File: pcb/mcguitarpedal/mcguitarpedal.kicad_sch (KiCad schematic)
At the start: 52 parts, among them J1 IN, J10 ENCODER2, J11 ENCODER3, J2 PREAMP_HEADERS, J3 BTN_MTX, J4 OUT, J5 EXP, J6 ILI9488 Module, J7 PWR_IN, J8 POT_HP_VOLUME_10k, J9 ENCODER1, SW1 SW_BYPASS, SW5 SW_TUNER, SW6 SW_PRESET, U1 Teensy4.0_AudioShield_REVD, U2 Teensy4.1, U4 74HC148, U5 74HC4094, U6 STPDWN-3P-5V, U7 STDN-3A24-ADJ

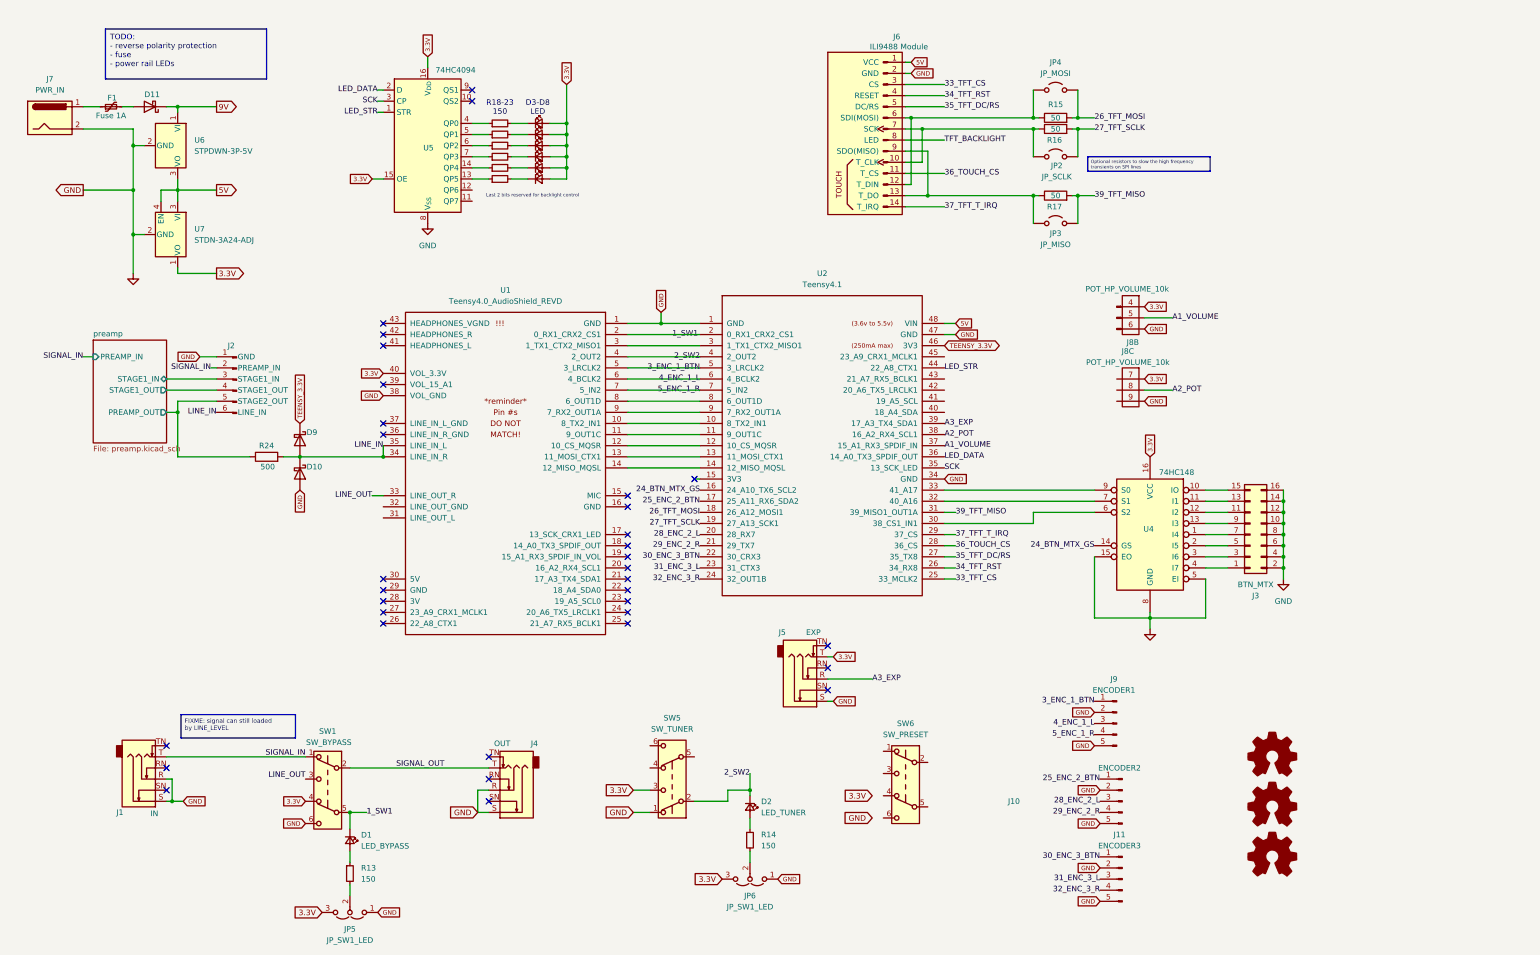
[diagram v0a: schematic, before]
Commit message: HCT595, audio shield sockets
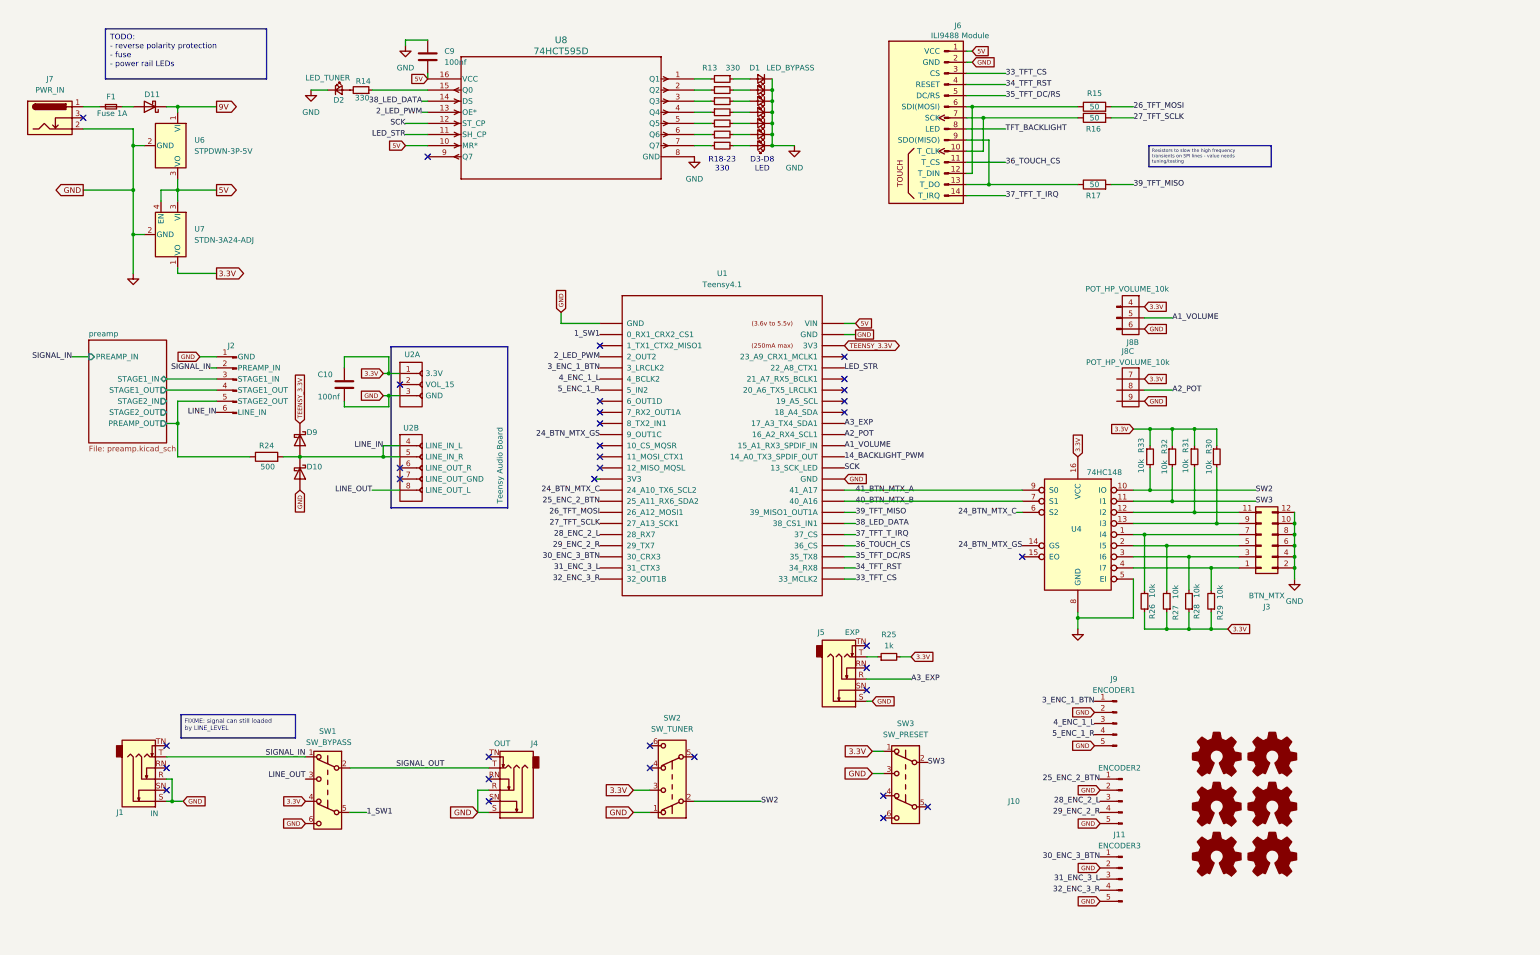
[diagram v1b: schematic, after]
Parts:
- removed D3: LED, LED_THT:LED_D3.0mm, symbol Device:LED_Small
- removed JP2: JP_SCLK, Connector_PinHeader_2.54mm:PinHeader_1x02_P2.54mm_Vertical, symbol Jumper:Jumper_2_Open
- removed JP3: JP_MISO, Connector_PinHeader_2.54mm:PinHeader_1x02_P2.54mm_Vertical, symbol Jumper:Jumper_2_Open
- removed JP4: JP_MOSI, Connector_PinHeader_2.54mm:PinHeader_1x02_P2.54mm_Vertical, symbol Jumper:Jumper_2_Open
- removed JP5, JP6: JP_SW1_LED, Connector_PinHeader_2.54mm:PinHeader_1x03_P2.54mm_Vertical, symbol Jumper:Jumper_3_Open
- removed U1: Teensy4.0_AudioShield_REVD, teensy_audio_shield:4.0audioshield_reference, symbol Audio board:Teensy4.0_AudioShield_REVD
- removed U5: 74HC4094, TI_FOOTPRINTS:N16, symbol 4xxx:HEF4094B
- added C10, C9: 100nf, Capacitor_THT:C_Rect_L7.2mm_W2.5mm_P5.00mm_FKS2_FKP2_MKS2_MKP2, symbol Device:C
- added D6: LED, mcguitarpedal:LED_D3.0mm, symbol Device:LED_Small
- added ENC1, ENC2, ENC3: Logo_Open_Hardware_Small, mcguitarpedal:Floating Encoder, symbol Graphic:Logo_Open_Hardware_Small
- added R25: 1k, Resistor_THT:R_Axial_DIN0207_L6.3mm_D2.5mm_P7.62mm_Horizontal, symbol Device:R_Small
- added R26, R27, R28, R29, R30, R31, R32, R33: 10k, Resistor_SMD:R_1206_3216Metric_Pad1.30x1.75mm_HandSolder, symbol Device:R_Small
- added U2: Teensy Audio Board, mcguitarpedal:4.0audioshield, symbol mcguitarpedal:Teensy_Audio_Board_Secondary_Sockets
- added U8: 74HCT595D, TI_FOOTPRINTS:SOT109-1_NEX, symbol 74HCT595:74HCT595D
- D3: renamed from D6; footprint LED_THT:LED_D3.0mm -> mcguitarpedal:LED_D3.0mm
- D4: renamed from D5; footprint LED_THT:LED_D3.0mm -> mcguitarpedal:LED_D3.0mm
- D5: renamed from D4; footprint LED_THT:LED_D3.0mm -> mcguitarpedal:LED_D3.0mm
- D7, D8: footprint LED_THT:LED_D3.0mm -> mcguitarpedal:LED_D3.0mm
- F1: footprint (none) -> Fuse:Fuse_Littelfuse_395Series; symbol Device:Polyfuse_Small -> Device:Fuse_Small
- J3: footprint Connector_PinHeader_2.54mm:PinHeader_2x08_P2.54mm_Vertical -> Connector_PinHeader_2.54mm:PinHeader_2x06_P2.54mm_Vertical; symbol Connector_Generic:Conn_02x08_Odd_Even -> Connector_Generic:Conn_02x06_Odd_Even
- J7: symbol Connector:Barrel_Jack -> Connector:Barrel_Jack_Switch
- R13, R14, R22, R23: value 150 -> 330
- R18: renamed from R21; value 150 -> 330
- R19: renamed from R20; value 150 -> 330
- R20: renamed from R19; value 150 -> 330
- R21: renamed from R18; value 150 -> 330
- renumbered SW5 to SW2, SW6 to SW3, U2 to U1
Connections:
- net 1_SW1: no longer D1.1 (K)
- net 24_BTN_MTX_GS: now also U1.11 (9_OUT1C); no longer U1.16 (24_A10_TX6_SCL2)
- net 3.3V: now also SW3.1 (A), C10.1, R25.2, R26.1, R27.1, R28.1, R29.1, R30.1, R31.1, R32.1, R33.1, U2.1 (3.3V); no longer D3.2 (A), D4.2 (A), D5.2 (A), D7.2 (A), D8.2 (A), J5.T
- net 5V: now also C9.2, U8.10 (MR*), U8.16 (VCC)
- net GND: now also D1.1 (K), D2.1 (K), D3.1 (K), D4.1 (K), D5.1 (K), D7.1 (K), D8.1 (K), SW3.3 (C), C10.2, C9.1, D6.1 (K), U2.3 (GND), U8.8 (GND); no longer J3.14 (Pin_14), J3.16 (Pin_16), U4.15 (EO)
- net LED_STR: now also U8.11 (SH_CP)
- net LINE_IN: now also U2.4 (LINE_IN_L), U2.5 (LINE_IN_R)
- net LINE_OUT: now also U2.8 (LINE_OUT_L)
- net SCK: now also U8.12 (ST_CP)
- net at D2.2 (A): now also R14.2; no longer R14.1
- net at R18.1: now also U8.7 (Q7)
- net at R18.2: now also D3.2 (A); no longer D3.1 (K)
- net at R22.1: now also U8.3 (Q3)
- net at R22.2: now also D7.2 (A); no longer D7.1 (K)
- net at R20.1: now also U8.5 (Q5)
- net at R20.2: now also D5.2 (A); no longer D5.1 (K)
- net SW3: now reaches SW3.2 (B)
- net SW3: now also U4.11 (I1), R32.2
- net at R13.2: now also U8.1 (Q1)
- net at R23.1: now also U8.2 (Q2)
- net at R23.2: now also D8.2 (A); no longer D8.1 (K)
- net 24_BTN_MTX_C: now reaches U4.6 (S2)
- net 24_BTN_MTX_C: now also U1.16 (24_A10_TX6_SCL2); no longer U1.30 (38_CS1_IN1)
- net 40_BTN_MTX_B: now reaches U1.32 (40_A16), U4.7 (S1)
- net 41_BTN_MTX_A: now reaches U1.33 (41_A17), U4.9 (S0)
- net at R21.1: now also U8.4 (Q4)
- net at R19.1: now also U8.6 (Q6)
- net at R19.2: now also D4.2 (A); no longer D4.1 (K)
- net at J3.7 (Pin_7), U4.1 (I4): now also R26.2
- net SW2: now reaches U4.10 (IO)
- net SW2: now also SW2.2 (B), R33.2; no longer J3.15 (Pin_15)
- net at J3.11 (Pin_11), U4.12 (I2): now also R31.2
- net at J3.9 (Pin_9), U4.13 (I3): now also R30.2
- net at J3.5 (Pin_5), U4.2 (I5): now also R27.2
- net at J3.3 (Pin_3), U4.3 (I6): now also R28.2
- net at J3.1 (Pin_1), U4.4 (I7): now also R29.2
- net at R21.2: now also D6.2 (A)
- removed net 2_SW2: D2.1 (K), SW2.2 (B), U1.4 (2_OUT2)
- net LED_DATA renamed 14_BACKLIGHT_PWM
- new net: R14.1, U8.15 (Q0)
- new net: J5.T, R25.1
- new net 2_LED_PWM: U1.4 (2_OUT2), U8.13 (OE*)
- new net 38_LED_DATA: U1.30 (38_CS1_IN1), U8.14 (DS)
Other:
- sheet preamp ports: added STAGE2_IN, STAGE2_OUT; removed none
- note added: "R18-23 330"
- note removed: "R18-23 150"
- moved on the sheet: D1, D2, J5, J6, R13, R14, R15, R16, R17, U4

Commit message: Miniaturization
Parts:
- added Q1: 2N7002K, Package_TO_SOT_SMD:SOT-23, symbol Transistor_FET:2N7002K
- added R36, R37, R38: 100, Resistor_THT:R_Axial_DIN0207_L6.3mm_D2.5mm_P7.62mm_Horizontal, symbol Device:R_Small
- added SW5, SW6: SW_PWR, Connector_PinHeader_2.54mm:PinHeader_1x02_P2.54mm_Vertical, symbol Switch:SW_SPST
- U6: footprint Package_TO_SOT_THT:TO-220-3_Vertical -> Package_TO_SOT_THT:TO-220-3_Horizontal_TabDown
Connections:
- net 14_BACKLIGHT_PWM: now also R37.1
- net 5V: now also SW6.2 (B)
- net GND: now also Q1.2 (S)
- net TFT_BACKLIGHT: now also R38.2
- net at F1.1: now also SW5.2 (B); no longer J7.1
- new net: R38.1, SW6.1 (A)
- new net: Q1.1 (G), R37.2
- new net: Q1.3 (D), R36.1
- new net: J7.1, SW5.1 (A)
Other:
- moved on the sheet: D11, D2, F1, J7, R14, U6, U7

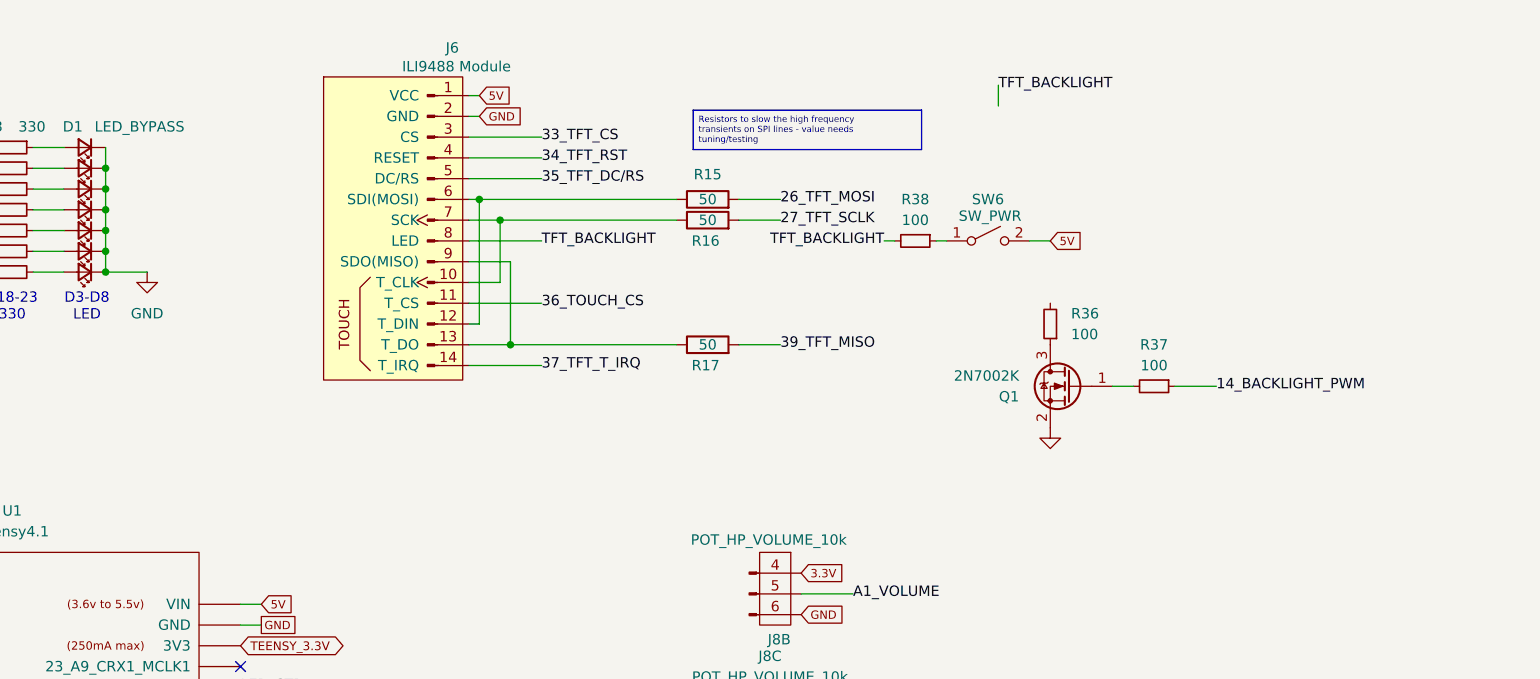
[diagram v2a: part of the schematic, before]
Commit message: Display backlight control schematic
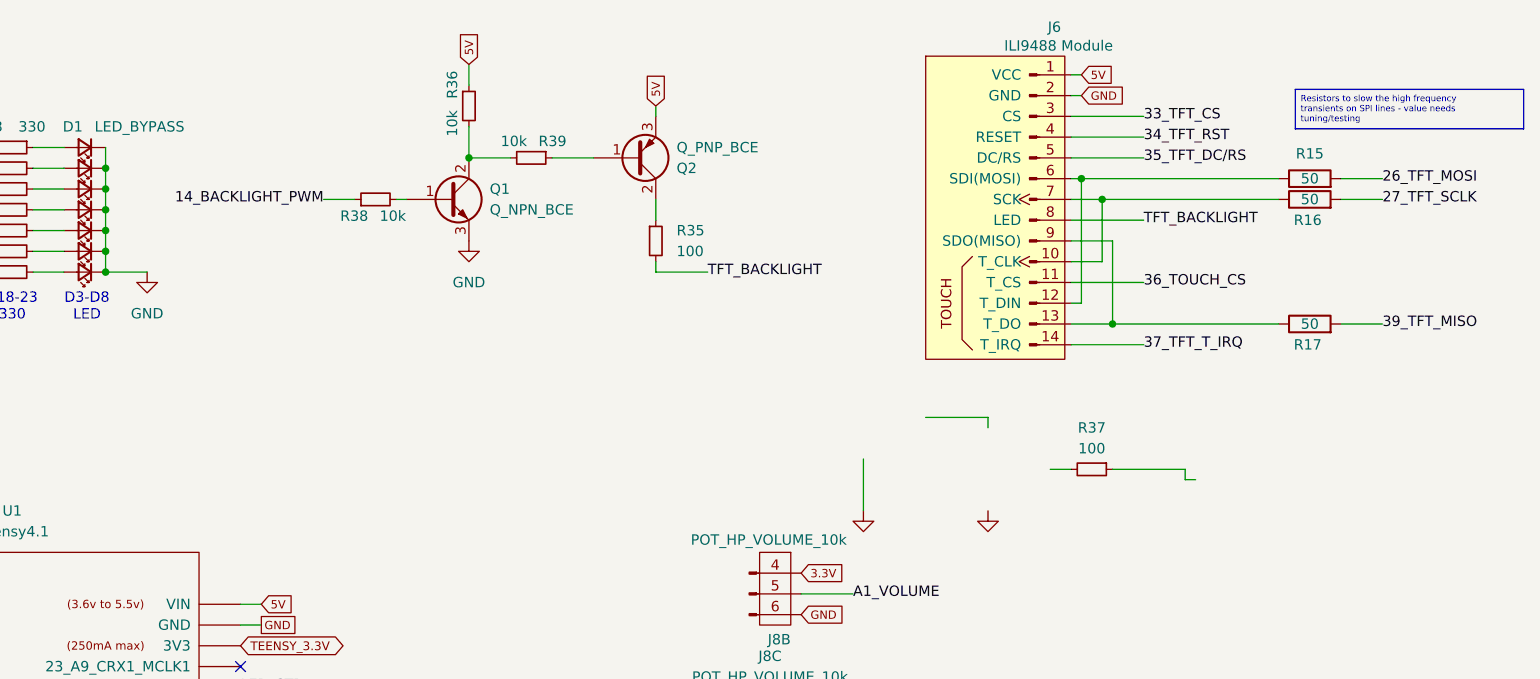
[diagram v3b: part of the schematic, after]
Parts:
- removed Q1: 2N7002K, Package_TO_SOT_SMD:SOT-23, symbol Transistor_FET:2N7002K
- removed SW6: SW_PWR, Connector_PinHeader_2.54mm:PinHeader_1x02_P2.54mm_Vertical, symbol Switch:SW_SPST
- added Q1: Q_NPN_BCE, symbol Device:Q_NPN_BCE
- added Q2: Q_PNP_BCE, symbol Device:Q_PNP_BCE
- added R35: 100, Resistor_THT:R_Axial_DIN0207_L6.3mm_D2.5mm_P7.62mm_Horizontal, symbol Device:R_Small
- added R39: 10k, Resistor_SMD:R_1206_3216Metric_Pad1.30x1.75mm_HandSolder, symbol Device:R_Small
- R36, R38: value 100 -> 10k; footprint Resistor_THT:R_Axial_DIN0207_L6.3mm_D2.5mm_P7.62mm_Horizontal -> Resistor_SMD:R_1206_3216Metric_Pad1.30x1.75mm_HandSolder
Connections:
- net 14_BACKLIGHT_PWM: now also R38.1; no longer R37.1
- net 5V: now also R36.1, Q2.3 (E)
- net GND: now also Q1.3 (E)
- net TFT_BACKLIGHT: now also R35.2; no longer R38.2
- net at R36.2: now also Q1.2 (C), R39.2
- new net: Q1.1 (B), R38.2
- new net: Q2.1 (B), R39.1
- new net: Q2.2 (C), R35.1
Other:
- moved on the sheet: J6, R15, R16, R17, R37
